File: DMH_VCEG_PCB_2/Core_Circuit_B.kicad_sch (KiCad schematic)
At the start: 103 parts, among them J24 Conn_01x06_PinHeader, J25 Conn_01x10_PinHeader, J26 Conn_01x10_PinHeader, Q17 BC558, Q18 BC558, Q19 BC548, Q20 BC548, Q21 MMBFJ113, Q22 MMBFJ113, Q23 BC548, Q24 BC548, Q25 BC548, Q26 BC548, SW4 SW_DPDT_x2, SW5 SW_DPDT_x2_On-Off-(On), U11 TL074, U12 4001, U13 40106, U14 CD4066BE, U15 TL074, U16 4001, U17 TL074, U24 CD4066BE

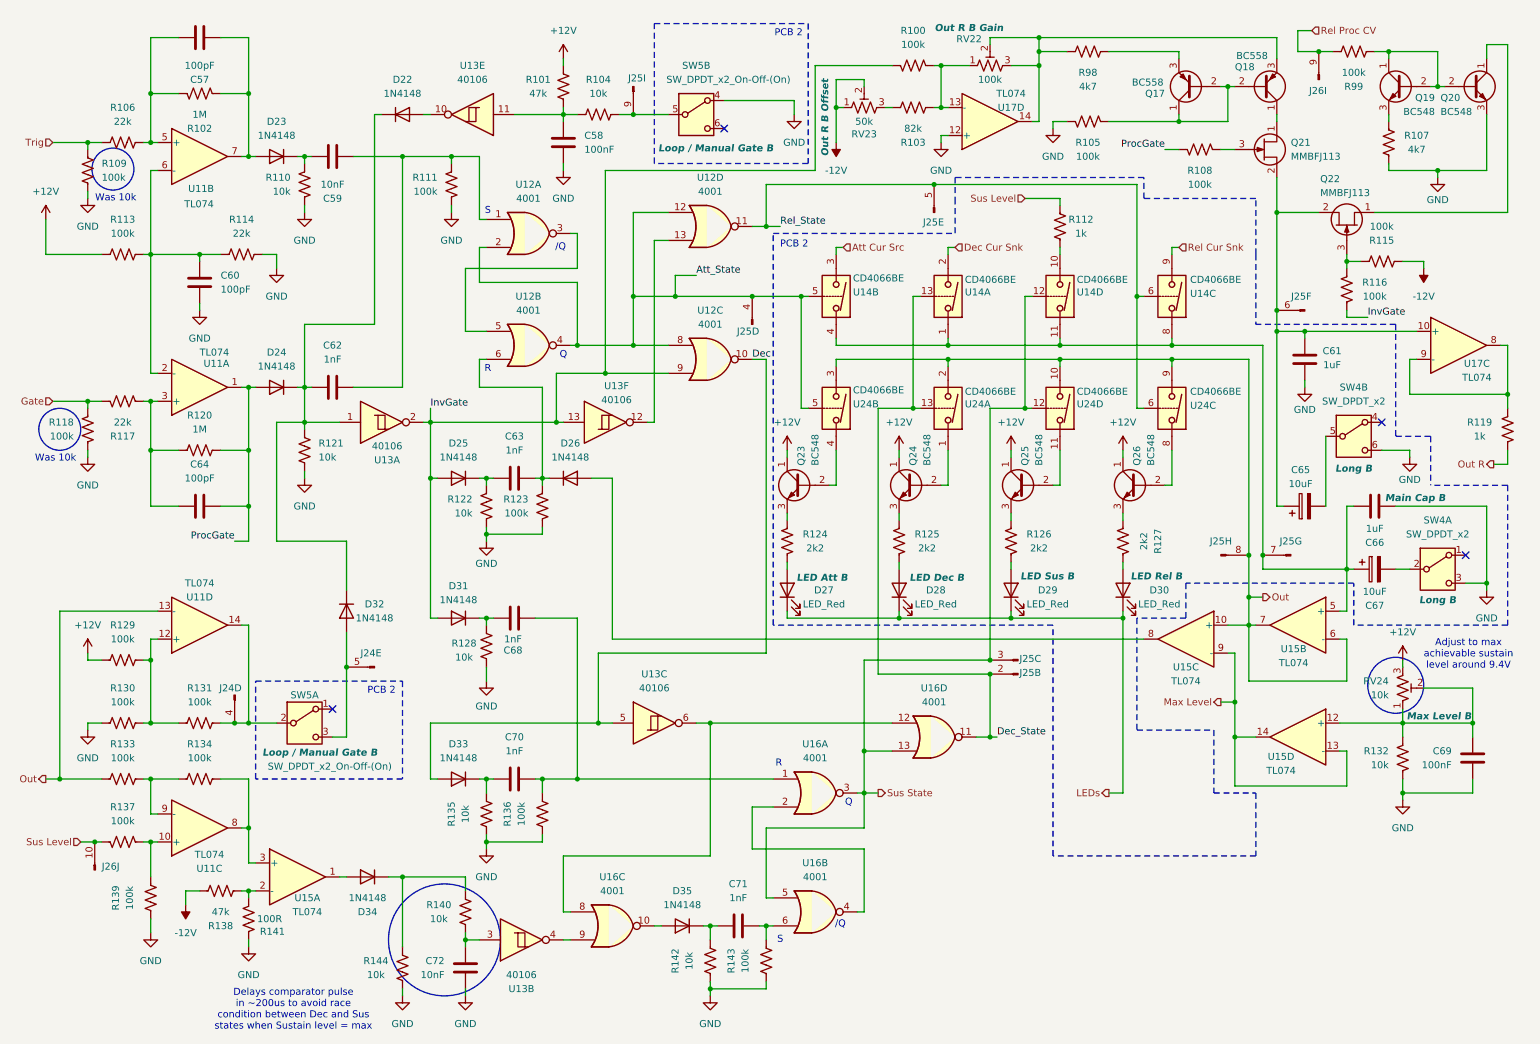
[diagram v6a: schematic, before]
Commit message: PCB 2 placement in progress
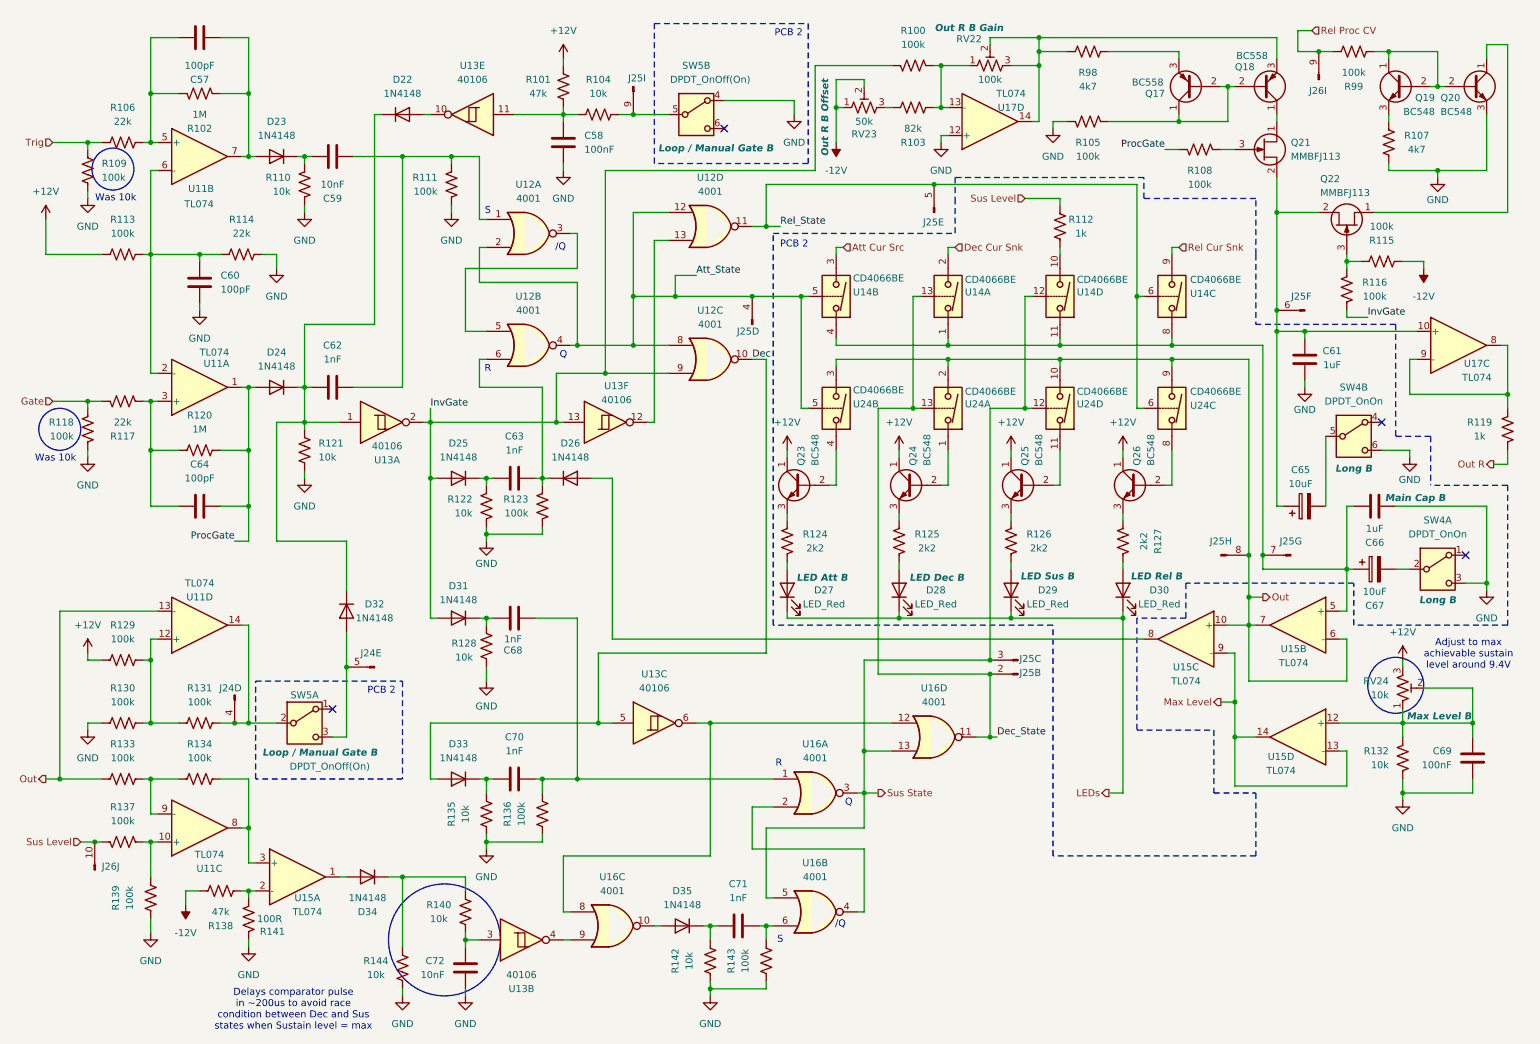
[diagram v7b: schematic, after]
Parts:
- SW4: value SW_DPDT_x2 -> DPDT_OnOn
- SW5: value SW_DPDT_x2_On-Off-(On) -> DPDT_OnOff(On)
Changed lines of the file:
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@@
 		)
 		(fill
-			(type color)
-			(color 255 206 244 1)
+			(type none)
 		)
 	)
@@
 			)
 		)
-		(property "Value" "SW_DPDT_x2_On-Off-(On)"
-			(at 141.732 24.13 0)
+		(property "Value" "DPDT_OnOff(On)"
+			(at 138.43 24.13 0)
 			(effects
 				(font
@@
 			)
 		)
-		(property "Value" "SW_DPDT_x2"
+		(property "Value" "DPDT_OnOn"
 			(at 255.27 82.55 0)
 			(effects
@@
 			)
 		)
-		(property "Value" "SW_DPDT_x2"
+		(property "Value" "DPDT_OnOn"
 			(at 270.51 106.68 0)
 			(effects
@@
 			)
 		)
-		(property "Value" "SW_DPDT_x2_On-Off-(On)"
+		(property "Value" "DPDT_OnOff(On)"
 			(at 69.342 148.844 0)
 			(effects

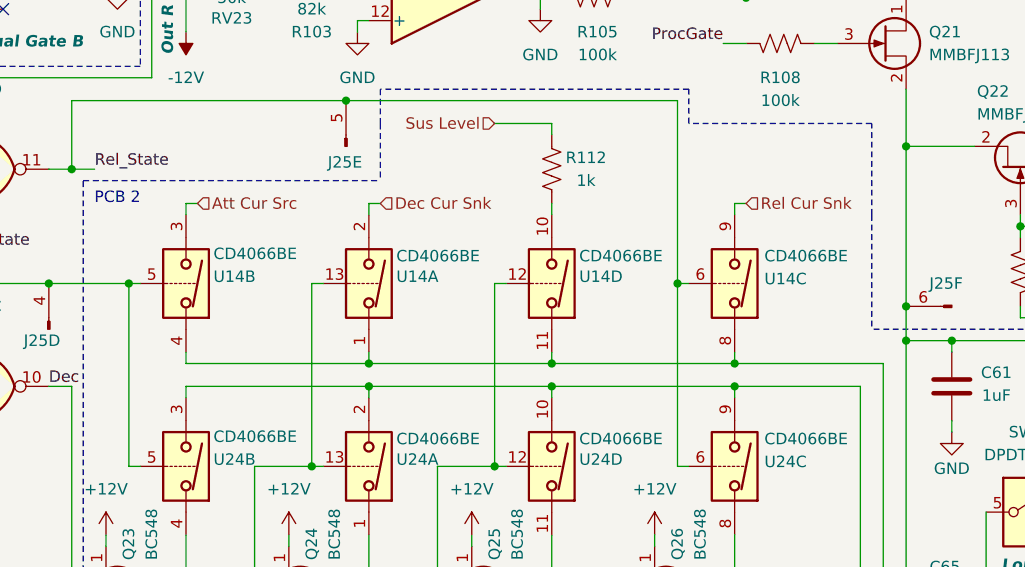
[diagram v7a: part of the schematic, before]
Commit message: Small changes during breadboarding
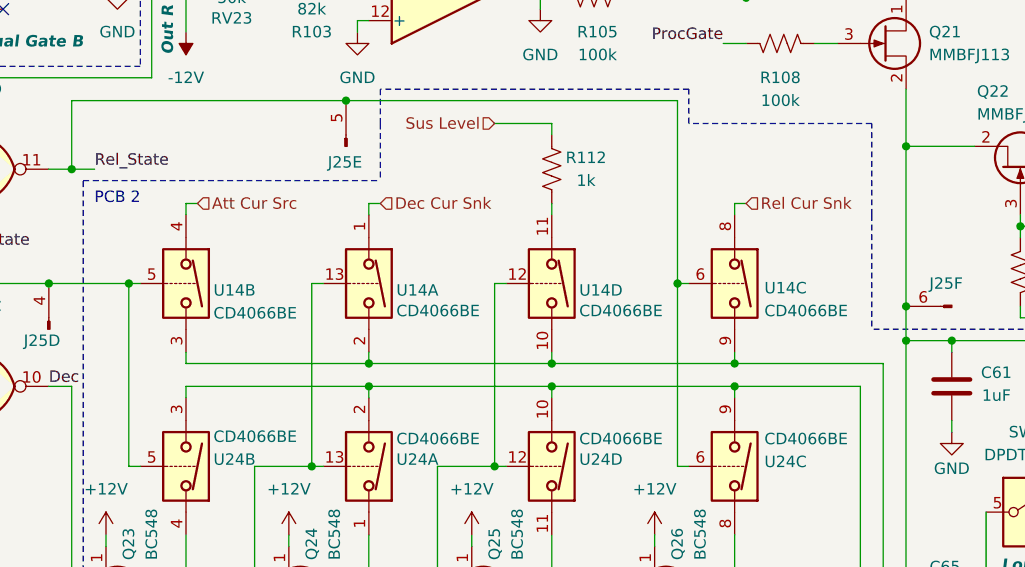
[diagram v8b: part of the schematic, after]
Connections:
- net Att Cur Src: now also U14.4; no longer U14.3
- net Dec Cur Snk: now also U14.1; no longer U14.2
- net Rel Cur Snk: now also U14.8; no longer U14.9
- net at C66.1, C67.1, J25.7 (Pin_7)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: now also U14.10, U14.2, U14.3, U14.9; no longer U14.1, U14.11, U14.4, U14.8
- net at R112.1: now also U14.11; no longer U14.10
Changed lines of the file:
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@@
 		(lib_id "Analog_Switch:CD4066BE")
 		(at 161.29 63.5 270)
-		(mirror x)
 		(unit 2)
 		(exclude_from_sim no)
@@
 		(dnp no)
 		(property "Reference" "U14"
-			(at 164.338 62.738 90)
+			(at 164.338 64.262 90)
 			(effects
 				(font
@@
 		)
 		(property "Value" "CD4066BE"
-			(at 164.338 60.198 90)
+			(at 164.338 66.802 90)
 			(effects
 				(font
@@
 		(lib_id "Analog_Switch:CD4066BE")
 		(at 181.61 63.5 270)
-		(mirror x)
 		(unit 1)
 		(exclude_from_sim no)
@@
 		(dnp no)
 		(property "Reference" "U14"
-			(at 184.658 62.738 90)
+			(at 184.658 64.262 90)
 			(effects
 				(font
@@
 		)
 		(property "Value" "CD4066BE"
-			(at 184.658 60.4521 90)
+			(at 184.658 66.5479 90)
 			(effects
 				(font
@@
 		(lib_id "Analog_Switch:CD4066BE")
 		(at 222.25 63.5 270)
-		(mirror x)
 		(unit 3)
 		(exclude_from_sim no)
@@
 		(dnp no)
 		(property "Reference" "U14"
-			(at 225.552 62.992 90)
+			(at 225.552 64.008 90)
 			(effects
 				(font
@@
 		)
 		(property "Value" "CD4066BE"
-			(at 225.552 60.452 90)
+			(at 225.552 66.548 90)
 			(effects
 				(font
@@
 		(lib_id "Analog_Switch:CD4066BE")
 		(at 201.93 63.5 270)
-		(mirror x)
 		(unit 4)
 		(exclude_from_sim no)
@@
 		(dnp no)
 		(property "Reference" "U14"
-			(at 204.978 62.738 90)
+			(at 204.978 64.262 90)
 			(effects
 				(font
@@
 		)
 		(property "Value" "CD4066BE"
-			(at 204.978 60.452 90)
+			(at 204.978 66.548 90)
 			(effects
 				(font
